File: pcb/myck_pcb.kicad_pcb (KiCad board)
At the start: 2 copper layers, 136.9 x 92.4 mm, 54 parts, among them SW1 SW_Push, SW10 SW_Push, SW11 SW_Push, SW12 SW_Push, SW13 SW_Push, SW14 SW_Push, SW15 SW_Push, SW16 SW_Push, SW17 SW_Push, SW18 SW_Push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

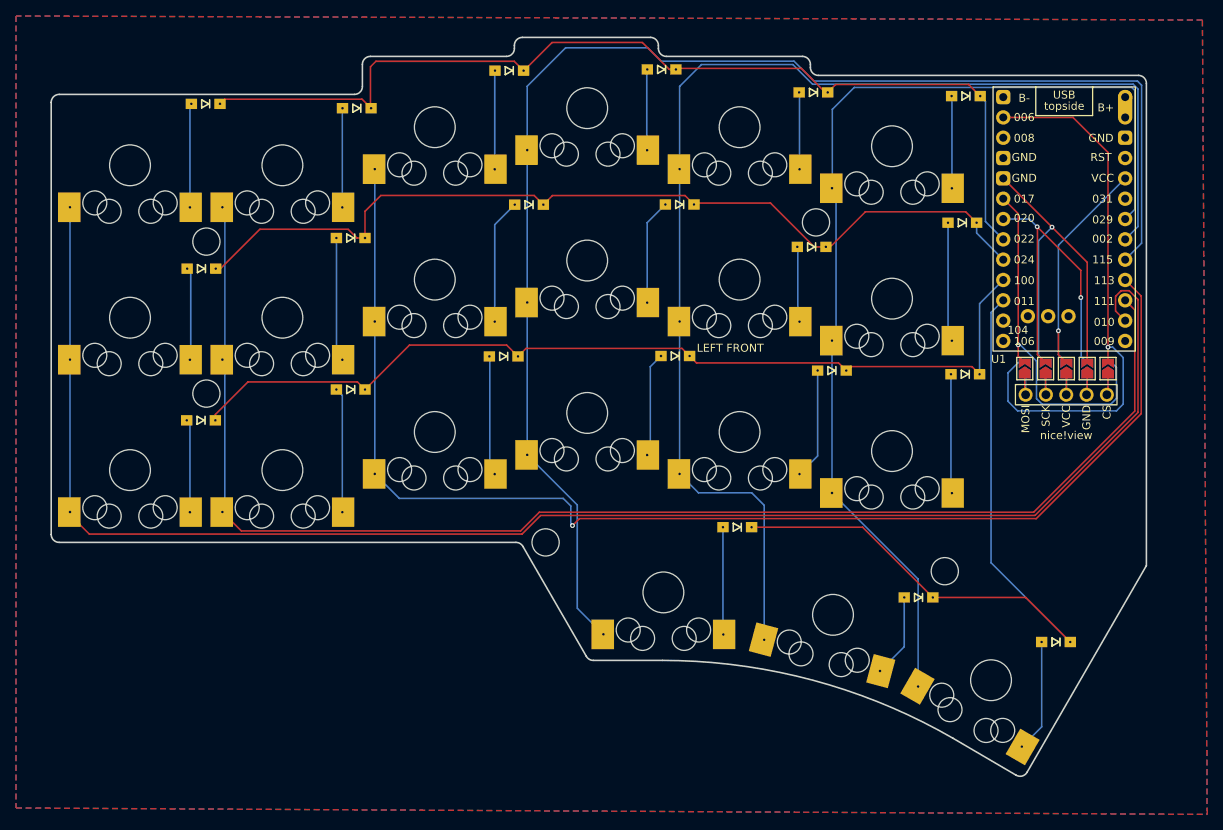
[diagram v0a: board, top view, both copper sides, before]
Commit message: Modificada la PCB
Para que sea más parecida a un teclado normal.

Dejado hueco para una batería más grande?
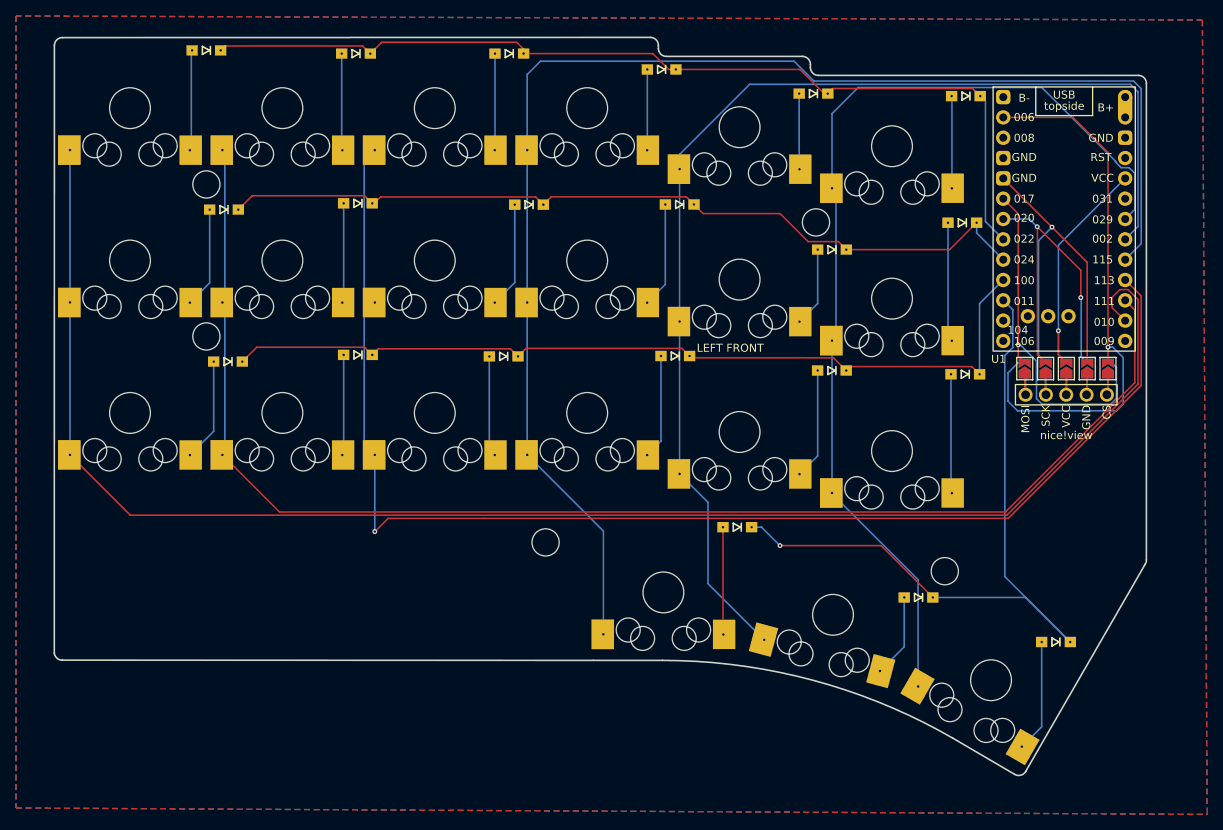
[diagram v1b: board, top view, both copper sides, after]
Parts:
- moved D13 8.08 mm to (107.5, 105.5)
- moved D7 7.90 mm to (107.0, 86.5)
- moved SW1 7.14 mm to (95.2, 73.8)
- moved SW2 7.14 mm to (114.3, 73.8)
- moved SW13 7.14 mm to (95.2, 111.9)
- moved SW14 7.14 mm to (114.3, 111.9)
- moved SW7 7.14 mm to (95.2, 92.9)
- moved SW8 7.14 mm to (114.3, 92.9)
- moved D2 6.83 mm to (123.5, 67.0)
- moved D1 6.68 mm to (104.8, 66.6)
- moved D14 4.42 mm to (123.7, 104.7)
- moved D8 4.42 mm to (123.7, 85.7)
- moved D11 2.57 mm to (183.0, 91.5)
- moved SW3 2.38 mm to (133.3, 73.8)
- moved SW15 2.38 mm to (133.3, 111.9)
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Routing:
- net Col4: track 156.6 -> 145.5 mm
- net Row1: track 113.9 -> 104.6 mm
- net Row0: track 126.1 -> 118.0 mm
- net Row2: track 116.4 -> 109.2 mm
- net Col5: track 132.7 -> 126.4 mm
- net Col2: track 161.2 -> 167.4 mm
- net Net-(D14-A): track 15.6 -> 12.6 mm
- net Net-(D8-A): track 15.5 -> 12.5 mm
- net Net-(D9-A): track 15.7 -> 13.3 mm
- net Net-(D15-A): track 15.0 -> 12.6 mm
- net Net-(D13-A): track 11.6 -> 12.9 mm
- net Col1: track 174.2 -> 173.1 mm
- net Net-(D7-A): track 11.6 -> 12.7 mm
- net Col3: track 175.8 -> 175.0 mm
- net Col0: track 200.4 -> 199.8 mm
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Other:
- board size 136.9 x 92.4 mm -> 136.5 x 92.3 mm
